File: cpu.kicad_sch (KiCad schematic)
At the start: 32 parts, among them IC101 HUC6280

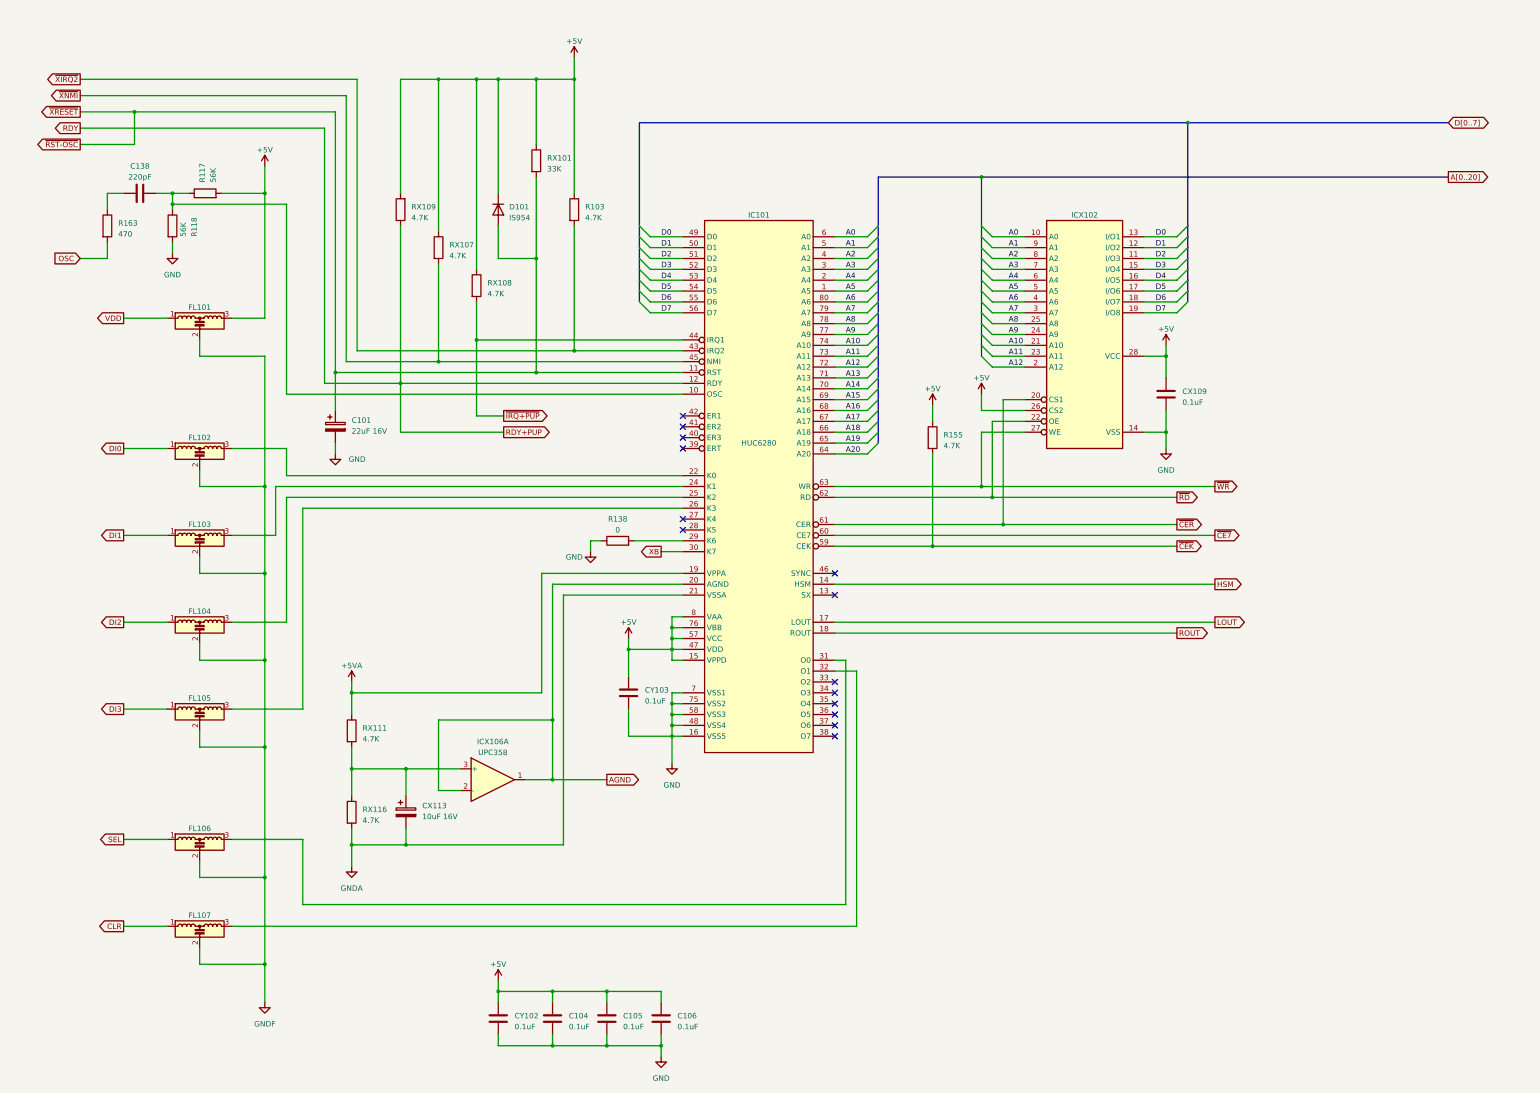
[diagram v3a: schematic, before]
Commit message: Finish basic routing, resolve DRC errors.
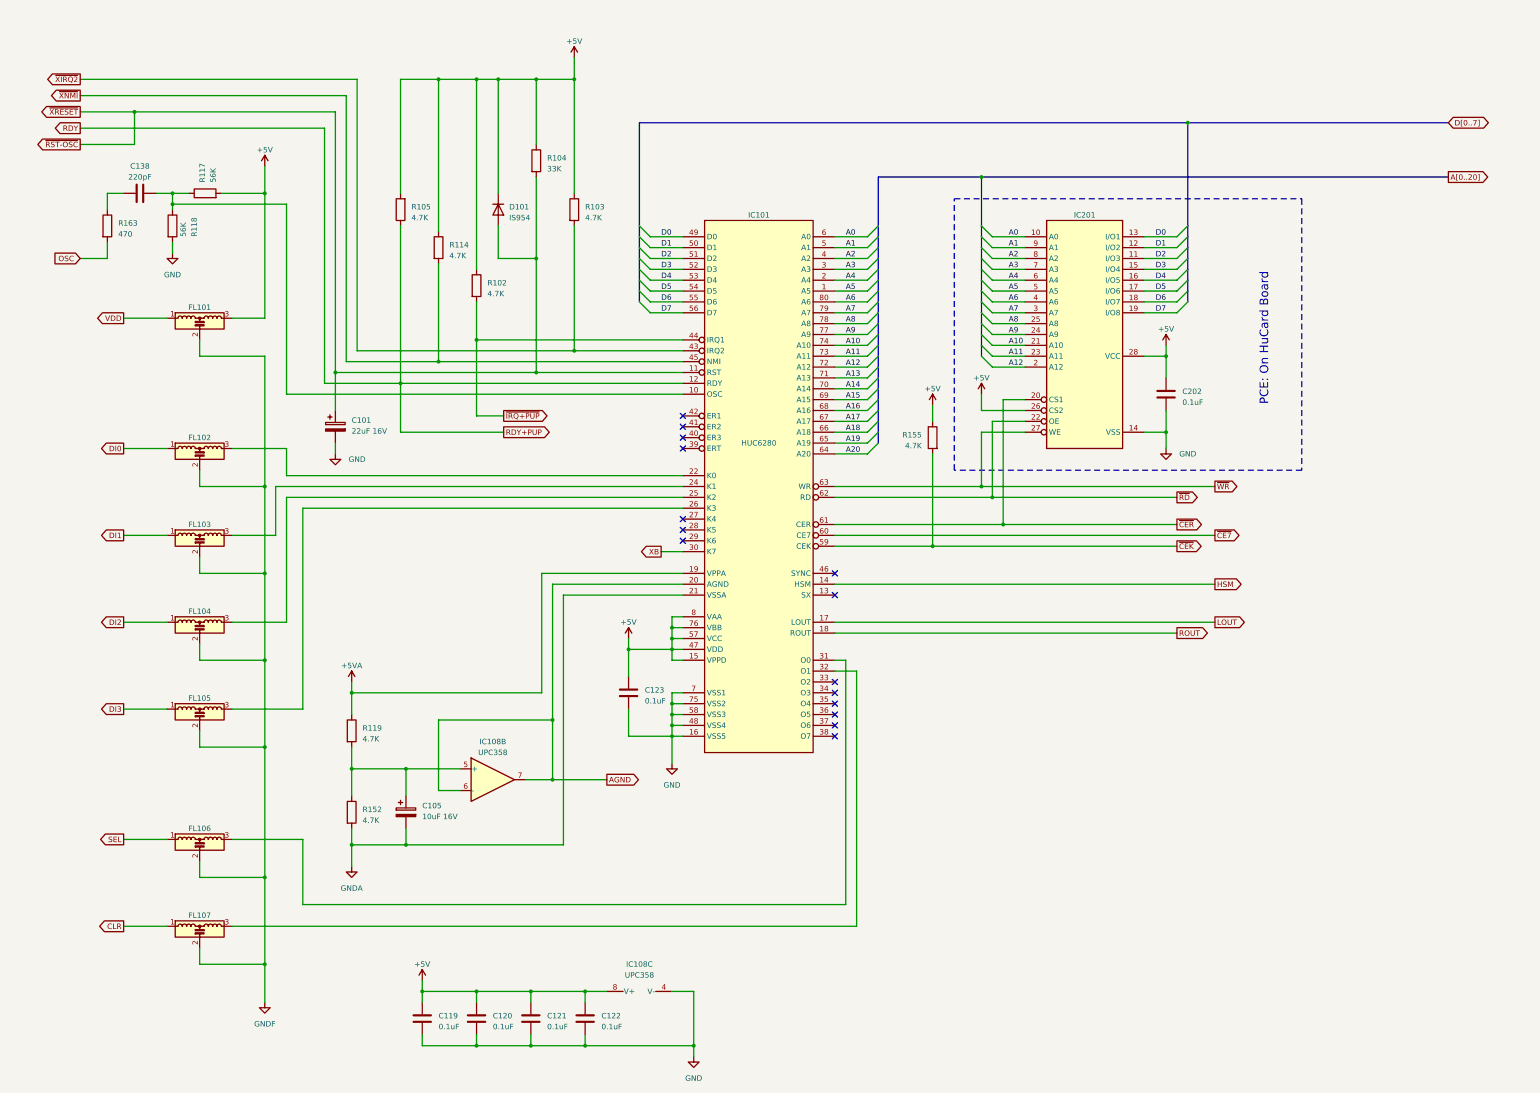
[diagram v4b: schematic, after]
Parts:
- removed C106: 0.1uF, A-PCENGINE:SMD_1206_C, symbol Device:C
- removed R138: 0, symbol Device:R
- added C122: 0.1uF, A-PCENGINE:SMD_1206_C, symbol Device:C
- added unit 3 of IC108
- C138: footprint A-PCENGINE:SMD_1206_C -> A-PCENGINE:SMD_1206
- C202: renamed from CX109; now left out of the parts list
- D101: footprint (none) -> A-PCENGINE:Diode_SMD
- IC108: renamed from ICX106; footprint (none) -> Package_DIP:DIP-8_W7.62mm_LongPads
- IC201: renamed from ICX102; now left out of the parts list
- R102: renamed from RX108; footprint (none) -> A-PCENGINE:SMD_1206
- R104: renamed from RX101; footprint (none) -> A-PCENGINE:SMD_1206
- R105: renamed from RX109; footprint (none) -> A-PCENGINE:SMD_1206
- R114: renamed from RX107; footprint (none) -> A-PCENGINE:SMD_1206
- R119: renamed from RX111; footprint (none) -> A-PCENGINE:SMD_1206
- R152: renamed from RX116; footprint (none) -> A-PCENGINE:SMD_1206
- renumbered CX113 to C105, CY102 to C119, C104 to C120, C105 to C121, CY103 to C123
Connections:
- net +5V: now also C122.1, IC108.8 (V+)
- net AGND: now also IC108.6 (-), IC108.7; no longer IC108.1, IC108.2 (-)
- net GND: now also C122.2, IC108.4 (V-)
- net at C105.1, R119.2, R152.1: now also IC108.5 (+); no longer IC108.3 (+)
- no-connect marks 14 -> 15
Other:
- note added: "PCE: On HuCard Board"
- moved on the sheet: C119, C120, C121

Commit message: First draft of complete PCB.
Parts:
- added C201: 10uF 16V, A-PCENGINE:Elec_P5.00mm, symbol Device:C_Polarized
- added C203, C204, C205, C206, C209, C211, C214, C215, C220: ?, A-PCENGINE:SMD_1206_C, symbol Device:C
- added C207, C208, C210, C212, C213, C216, C217, C218, C219: N/P, A-PCENGINE:SMD_1206_C, symbol Device:C
- IC108: value UPC358 -> μPC358C; footprint Package_DIP:DIP-8_W7.62mm_LongPads -> A-PCENGINE:DIP-8
- R155: value 4.7K -> 5.6K
- R163: value 470 -> 1.2K
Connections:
- net +5V: now also C201.1, C203.1, C204.1, C205.1, C206.1, C207.1, C208.1, C209.1, C210.1, C211.1, C212.1, C213.1, C214.1, C215.1, C216.1, C217.1, C218.1, C219.1, C220.1
- net A10: now also C210.2
- net A11: now also C207.2
- net A12: now also C219.2
- net A13: now also C206.2
- net A14: now also C205.2
- net A15: now also C214.2
- net A16: now also C215.2
- net A17: now also C204.2
- net A18: now also C203.2
- net A19: now also C220.2
- net A20: now also C211.2
- net A3: now also C216.2
- net A4: now also C217.2
- net A5: now also C212.2
- net A6: now also C218.2
- net A7: now also C213.2
- net A8: now also C209.2
- net A9: now also C208.2
- net GND: now also C201.2
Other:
- note added: "N/P = Not Populated"
- note added: "On HuCard Board"
- note removed: "PCE: On HuCard Board"
- moved on the sheet: C101, C105, C119, C120, C121, C122, C123, C138, C202, D101, FL101, FL102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

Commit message: Verify passive values.
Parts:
- C119, C121, C122: value 0.1uF -> 0.1uF L
- C123: value 0.1uF -> 0.1uf
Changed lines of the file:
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@@
       (effects (font (size 1.27 1.27)) (justify left))
     )
-    (property "Value" "0.1uF" (at 135.89 249.555 0)
+    (property "Value" "0.1uF L" (at 135.89 249.555 0)
       (effects (font (size 1.27 1.27)) (justify left))
     )
@@
       (effects (font (size 1.27 1.27)) (justify left))
     )
-    (property "Value" "0.1uF" (at 184.15 173.355 0)
+    (property "Value" "0.1uf" (at 184.15 173.355 0)
       (effects (font (size 1.27 1.27)) (justify left))
     )
@@
       (effects (font (size 1.27 1.27)) (justify left))
     )
-    (property "Value" "0.1uF" (at 161.29 249.555 0)
+    (property "Value" "0.1uF L" (at 161.29 249.555 0)
       (effects (font (size 1.27 1.27)) (justify left))
     )
@@
       (effects (font (size 1.27 1.27)) (justify left))
     )
-    (property "Value" "0.1uF" (at 173.99 249.555 0)
-      (effects (font (size 1.27 1.27)) (justify left))
-    )
+    (property "Value" "0.1uF L" (at 173.99 249.555 0)
+      (effects (font (size 1.27 1.27)) (justify left))
+    )

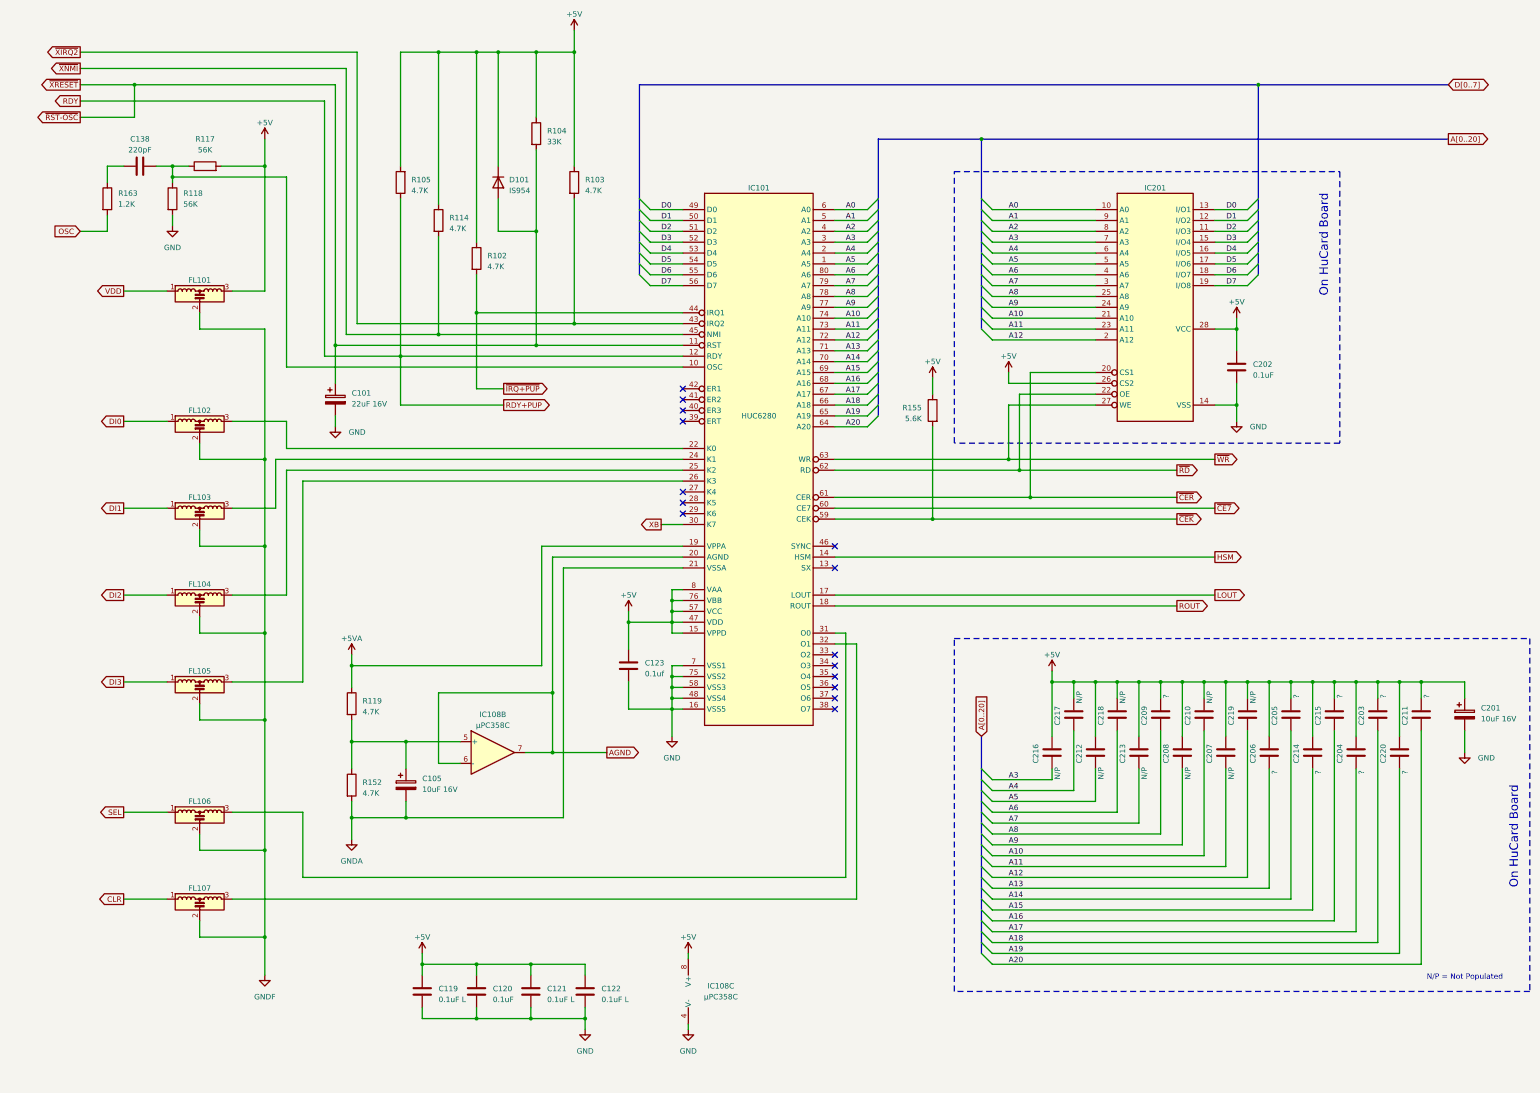
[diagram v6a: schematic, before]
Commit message: Silkscreen stuff, tidy schematics, corrections.
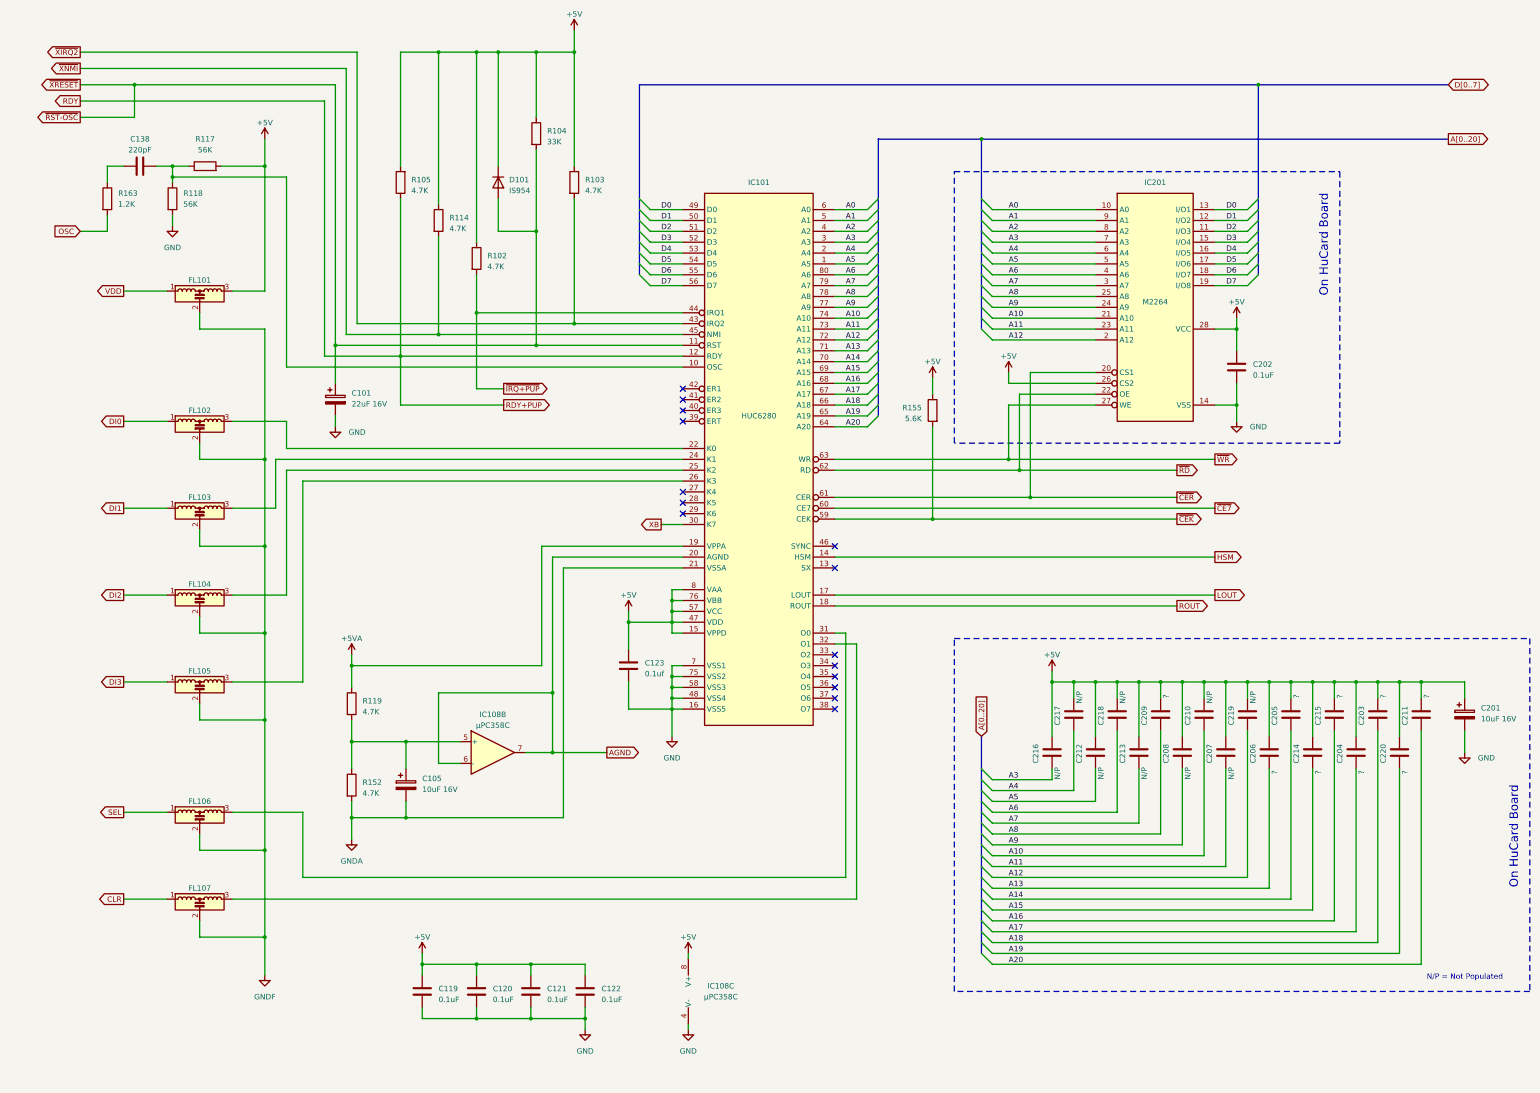
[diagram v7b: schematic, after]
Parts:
- C119, C121, C122: value 0.1uF L -> 0.1uF
- IC201: value ~ -> M2264
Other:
- title: (none) -> PC Engine CPU and RAM
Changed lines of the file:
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@@
 (kicad_sch (version 20230121) (generator eeschema)
   (paper "A3")
+  (title_block
+    (title "PC Engine CPU and RAM")
+    (date "2023-08-17")
+    (rev "1.0")
+    (comment 1 "Differences reverse engineered from original PWD-623A board")
+    (comment 2 "Adapted from existing TurboGrafx-16 schematics by Cosam")
+  )
   (junction (at 95.25 184.15) (diameter 0) (color 0 0 0 0)
   )
@@
       (effects (font (size 1.27 1.27)) (justify left))
     )
-    (property "Value" "0.1uF L" (at 135.89 249.555 0)
+    (property "Value" "0.1uF" (at 135.89 249.555 0)
       (effects (font (size 1.27 1.27)) (justify left))
     )
@@
   )
   (symbol (lib_id "PC-Engine:Hu6280") (at 210.82 120.65 0) (unit 1)
-    (in_bom yes) (on_board yes) (dnp no) (fields_autoplaced)
-    (property "Reference" "IC101" (at 210.82 59.69 0)
+    (in_bom yes) (on_board yes) (dnp no)
+    (property "Reference" "IC101" (at 210.82 58.42 0)
       (effects (font (size 1.27 1.27)))
     )
@@
       (effects (font (size 1.27 1.27)) (justify left))
     )
-    (property "Value" "0.1uF L" (at 161.29 249.555 0)
+    (property "Value" "0.1uF" (at 161.29 249.555 0)
       (effects (font (size 1.27 1.27)) (justify left))
     )
@@
   )
   (symbol (lib_id "PC-Engine:M2264") (at 303.53 58.42 0) (unit 1)
-    (in_bom no) (on_board no) (dnp no) (fields_autoplaced)
-    (property "Reference" "IC201" (at 303.53 59.69 0)
+    (in_bom no) (on_board no) (dnp no)
+    (property "Reference" "IC201" (at 303.53 58.42 0)
       (effects (font (size 1.27 1.27)))
     )
-    (property "Value" "~" (at 303.53 58.42 0)
+    (property "Value" "M2264" (at 303.53 86.36 0)
       (effects (font (size 1.27 1.27)))
     )
@@
       (effects (font (size 1.27 1.27)) (justify left))
     )
-    (property "Value" "0.1uF L" (at 173.99 249.555 0)
+    (property "Value" "0.1uF" (at 173.99 249.555 0)
       (effects (font (size 1.27 1.27)) (justify left))
     )
